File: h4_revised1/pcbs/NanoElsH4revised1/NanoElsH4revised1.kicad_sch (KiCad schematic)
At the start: 137 parts, among them Q1 SI2302ADS-T1, Q10 SI2302ADS-T1, Q11 SI2302ADS-T1, Q12 SI2302ADS-T1, Q13 SI2302ADS-T1, Q14 SI2302ADS-T1, Q15 SI2302ADS-T1, Q16 SI2302ADS-T1, Q18 SI2302ADS-T1, Q2 SI2302ADS-T1, Q3 S9013W, Q4 S9013W, Q5 SI2302ADS-T1, Q6 SI2302ADS-T1, Q7 SI2302ADS-T1, Q8 SI2302ADS-T1, Q9 SI2302ADS-T1

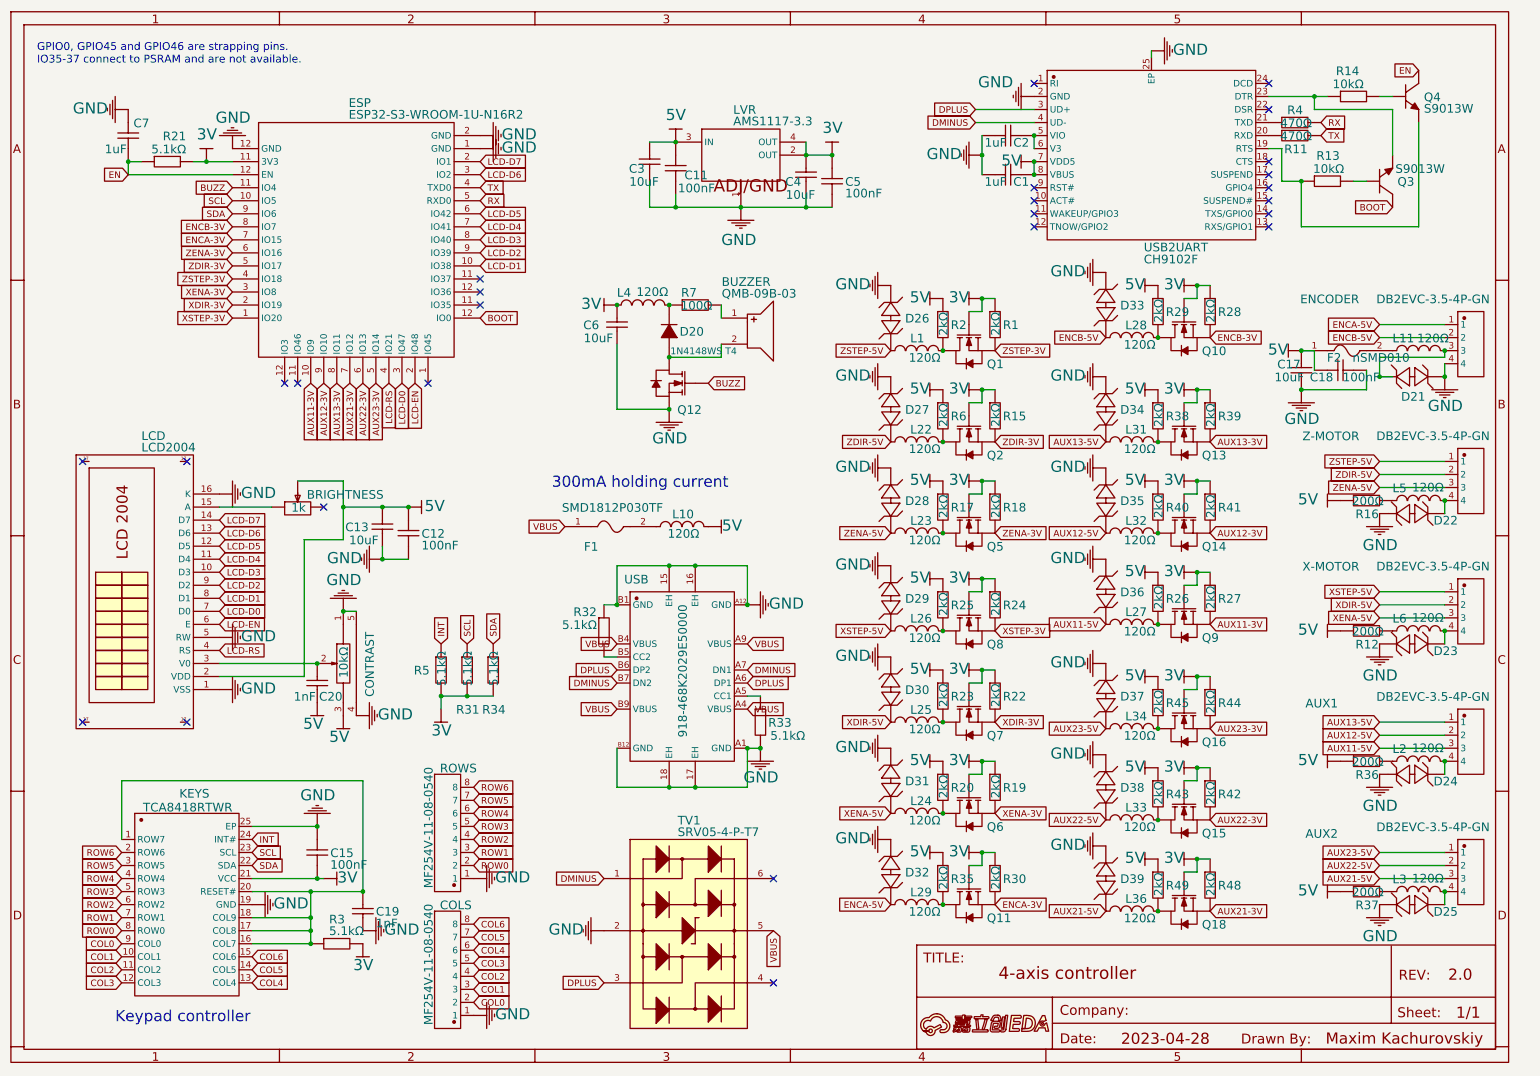
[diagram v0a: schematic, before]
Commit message: - Added actual KiCad 8 files (layout ready, but some cosmetic documentation ToDo's)
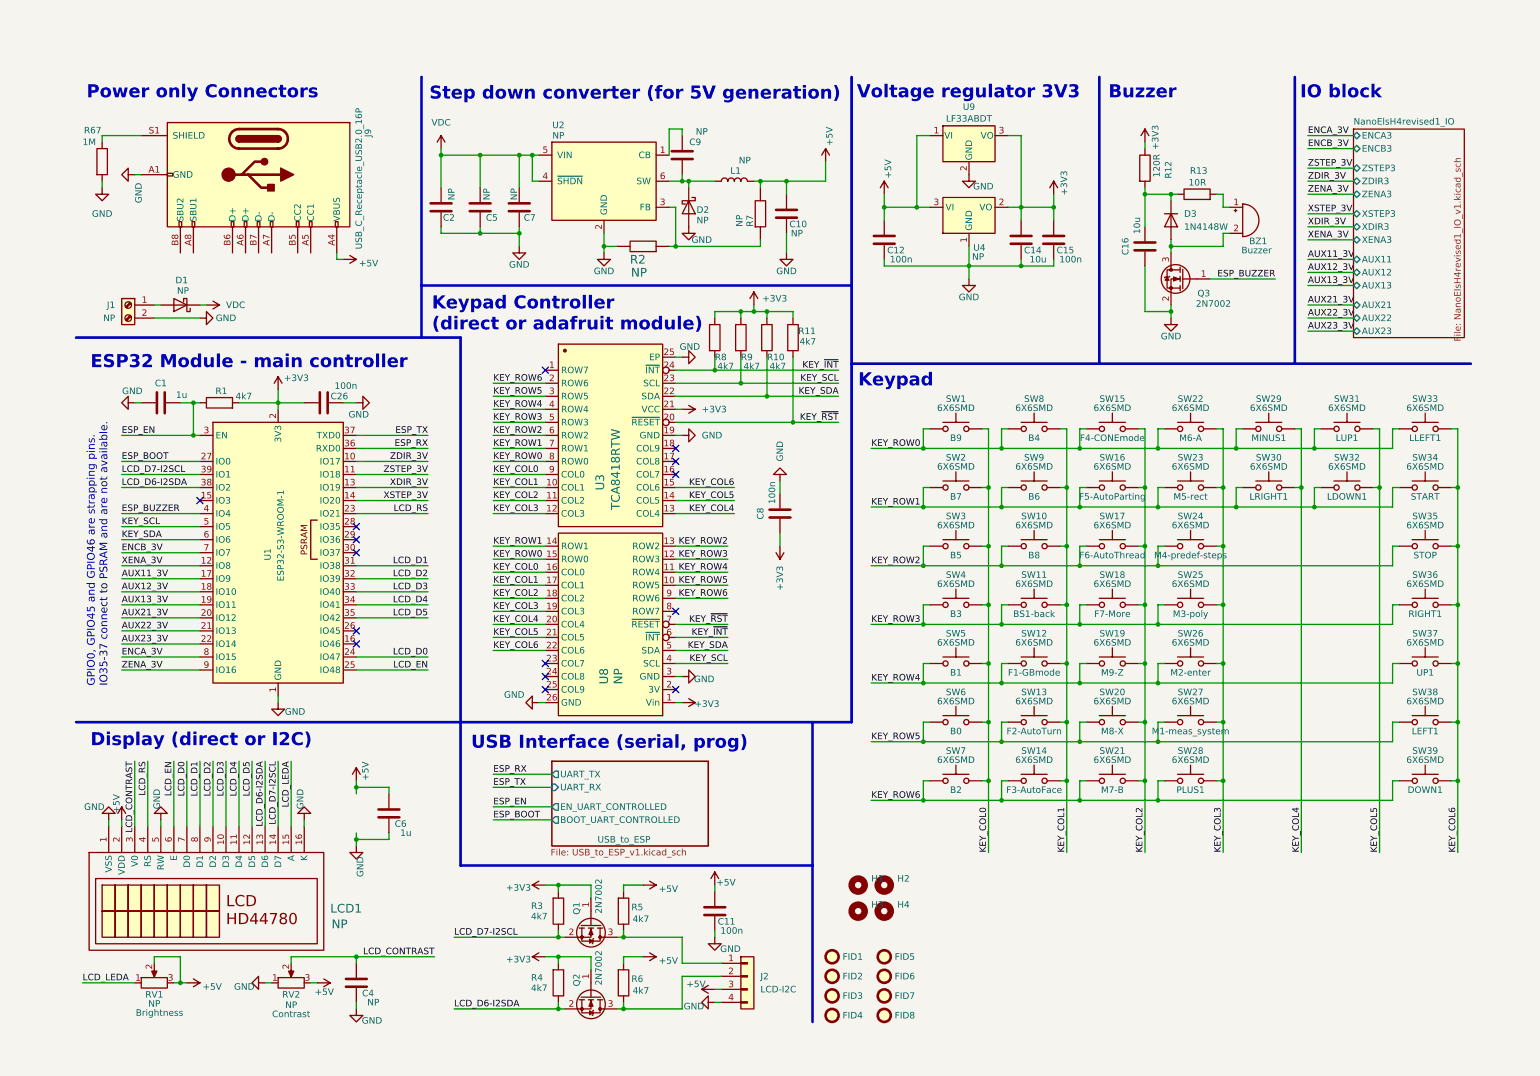
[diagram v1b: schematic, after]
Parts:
- removed A: A, symbol Unknown_10_-850
- removed AUX1: DB2EVC-3.5-4P-GN, symbol DB2EVC-3.5-4P-GN_3
- removed AUX2: DB2EVC-3.5-4P-GN, symbol DB2EVC-3.5-4P-GN_4
- removed BRIGHTNESS: 1k, symbol 3314G-2-102E
- removed BUZZER: QMB-09B-03, symbol QMB-09B-03
- removed C1: 1uF, symbol CL05A105KA5NQNC_2
- removed C11: 100nF, symbol CC0603KRX7R9BB104
- removed C12: 100nF, symbol CC0603KRX7R9BB104_3
- removed C13: 10uF, symbol CL31A106KBHNNNE_2
- removed C15: 100nF, symbol CC0603KRX7R9BB104_2
- removed C17: 10uF, symbol CL31A106KBHNNNE_3
- removed C18: 100nF, symbol CC0603KRX7R9BB104_4
- removed C19: 1nF, symbol 0402B102K500NT
- removed C2: 1uF, symbol CL05A105KA5NQNC_1
- removed C20: 1nF, symbol 0402B102K500NT_1
- removed C3: 10uF, symbol CL31A106KBHNNNE
- removed C4: 10uF, symbol CL31A106KBHNNNE_1
- removed C5: 100nF, symbol CC0603KRX7R9BB104_1
- removed C6: 10uF, symbol CL31A106KBHNNNE_4
- removed C7: 1uF, symbol CL05A105KA5NQNC
- removed COLS: MF254V-11-08-0540, symbol MF254V-11-08-0540_1
- removed CONTRAST: 10kΩ, symbol RK09K113004U
- removed D20: 1N4148WS T4, symbol 1N4148WS T4
- removed D21: KESD9B5VL, symbol KESD9B5VL
- removed D22: KESD9B5VL, symbol KESD9B5VL_1
- removed D23: KESD9B5VL, symbol KESD9B5VL_2
- removed D24: KESD9B5VL, symbol KESD9B5VL_3
- removed D25: KESD9B5VL, symbol KESD9B5VL_4
- removed D26: KESD9B5VL, symbol KESD9B5VL_5
- removed D27: KESD9B5VL, symbol KESD9B5VL_6
- removed D28: KESD9B5VL, symbol KESD9B5VL_7
- removed D29: KESD9B5VL, symbol KESD9B5VL_8
- removed D30: KESD9B5VL, symbol KESD9B5VL_9
- removed D31: KESD9B5VL, symbol KESD9B5VL_10
- removed D32: KESD9B5VL, symbol KESD9B5VL_11
- removed D33: KESD9B5VL, symbol KESD9B5VL_12
- removed D34: KESD9B5VL, symbol KESD9B5VL_13
- removed D35: KESD9B5VL, symbol KESD9B5VL_14
- removed D36: KESD9B5VL, symbol KESD9B5VL_15
- removed D37: KESD9B5VL, symbol KESD9B5VL_16
- removed D38: KESD9B5VL, symbol KESD9B5VL_17
- removed D39: KESD9B5VL, symbol KESD9B5VL_18
- removed ENCODER: DB2EVC-3.5-4P-GN, symbol DB2EVC-3.5-4P-GN_2
- removed ESP: ESP32-S3-WROOM-1U-N16R2, symbol ESP32-S3-WROOM-1U-N16R2
- removed F1: SMD1812P030TF, symbol SMD1812P030TF
- removed F2: nSMD010, symbol nSMD010
- removed KEYS: TCA8418RTWR, symbol TCA8418RTWR
- removed L1: 120Ω, symbol CBM160808U121T_4
- removed L10: 120Ω, symbol CBM160808U121T_3
- removed L11: 120Ω, symbol CBM160808U121T_2
- removed L2: 120Ω, symbol CBM160808U121T_18
- removed L22: 120Ω, symbol CBM160808U121T_5
- removed L23: 120Ω, symbol CBM160808U121T_6
- removed L24: 120Ω, symbol CBM160808U121T_7
- removed L25: 120Ω, symbol CBM160808U121T_8
- removed L26: 120Ω, symbol CBM160808U121T_9
- removed L27: 120Ω, symbol CBM160808U121T_12
- removed L28: 120Ω, symbol CBM160808U121T_10
- removed L29: 120Ω, symbol CBM160808U121T_11
- removed L3: 120Ω, symbol CBM160808U121T_19
- removed L31: 120Ω, symbol CBM160808U121T_13
- removed L32: 120Ω, symbol CBM160808U121T_14
- removed L33: 120Ω, symbol CBM160808U121T_15
- removed L34: 120Ω, symbol CBM160808U121T_16
- removed L36: 120Ω, symbol CBM160808U121T_17
- removed L4: 120Ω, symbol CBM160808U121T_20
- removed L5: 120Ω, symbol CBM160808U121T
- removed L6: 120Ω, symbol CBM160808U121T_1
- removed LCD: LCD2004, symbol LCD2004
- removed LVR: AMS1117-3.3, symbol AMS1117-3.3_C2992570
- removed Q1: SI2302ADS-T1, symbol SI2302ADS-T1
- removed Q10: SI2302ADS-T1, symbol SI2302ADS-T1_6
- removed Q11: SI2302ADS-T1, symbol SI2302ADS-T1_7
- removed Q12: SI2302ADS-T1, symbol SI2302ADS-T1_14
- removed Q13: SI2302ADS-T1, symbol SI2302ADS-T1_9
- removed Q14: SI2302ADS-T1, symbol SI2302ADS-T1_10
- removed Q15: SI2302ADS-T1, symbol SI2302ADS-T1_11
- removed Q16: SI2302ADS-T1, symbol SI2302ADS-T1_12
- removed Q18: SI2302ADS-T1, symbol SI2302ADS-T1_13
- removed Q2: SI2302ADS-T1, symbol SI2302ADS-T1_1
- removed Q3: S9013W, symbol S9013W
- removed Q4: S9013W, symbol S9013W_1
- removed Q5: SI2302ADS-T1, symbol SI2302ADS-T1_2
- removed Q6: SI2302ADS-T1, symbol SI2302ADS-T1_3
- removed Q7: SI2302ADS-T1, symbol SI2302ADS-T1_4
- removed Q8: SI2302ADS-T1, symbol SI2302ADS-T1_5
- removed Q9: SI2302ADS-T1, symbol SI2302ADS-T1_8
- removed R1: 2kΩ, symbol 0603WAF2001T5E_1
- removed R11: 470Ω, symbol 0603WAF4700T5E_1
- removed R12: 200Ω, symbol 0805W8F2000T5E_1
- removed R13: 10kΩ, symbol 0603WAF1002T5E
- removed R14: 10kΩ, symbol 0603WAF1002T5E_1
- removed R15: 2kΩ, symbol 0603WAF2001T5E_3
- removed R16: 200Ω, symbol 0805W8F2000T5E
- removed R17: 2kΩ, symbol 0603WAF2001T5E_4
- removed R18: 2kΩ, symbol 0603WAF2001T5E_5
- removed R19: 2kΩ, symbol 0603WAF2001T5E_6
- removed R2: 2kΩ, symbol 0603WAF2001T5E
- removed R20: 2kΩ, symbol 0603WAF2001T5E_7
- removed R21: 5.1kΩ, symbol 0603WAF5101T5E_6
- removed R22: 2kΩ, symbol 0603WAF2001T5E_8
- removed R23: 2kΩ, symbol 0603WAF2001T5E_9
- removed R24: 2kΩ, symbol 0603WAF2001T5E_10
- removed R25: 2kΩ, symbol 0603WAF2001T5E_11
- removed R26: 2kΩ, symbol 0603WAF2001T5E_16
- removed R27: 2kΩ, symbol 0603WAF2001T5E_17
- removed R28: 2kΩ, symbol 0603WAF2001T5E_12
- removed R29: 2kΩ, symbol 0603WAF2001T5E_13
- removed R3: 5.1kΩ, symbol 0603WAF5101T5E_5
- removed R30: 2kΩ, symbol 0603WAF2001T5E_14
- removed R31: 5.1kΩ, symbol 0603WAF5101T5E_3
- removed R32: 5.1kΩ, symbol 0603WAF5101T5E_1
- removed R33: 5.1kΩ, symbol 0603WAF5101T5E
- removed R34: 5.1kΩ, symbol 0603WAF5101T5E_4
- removed R35: 2kΩ, symbol 0603WAF2001T5E_15
- removed R36: 200Ω, symbol 0805W8F2000T5E_2
- removed R37: 200Ω, symbol 0805W8F2000T5E_3
- removed R38: 2kΩ, symbol 0603WAF2001T5E_18
- removed R39: 2kΩ, symbol 0603WAF2001T5E_19
- removed R4: 470Ω, symbol 0603WAF4700T5E
- removed R40: 2kΩ, symbol 0603WAF2001T5E_20
- removed R41: 2kΩ, symbol 0603WAF2001T5E_21
- removed R42: 2kΩ, symbol 0603WAF2001T5E_22
- removed R43: 2kΩ, symbol 0603WAF2001T5E_23
- removed R44: 2kΩ, symbol 0603WAF2001T5E_24
- removed R45: 2kΩ, symbol 0603WAF2001T5E_25
- removed R48: 2kΩ, symbol 0603WAF2001T5E_26
- removed R49: 2kΩ, symbol 0603WAF2001T5E_27
- removed R5: 5.1kΩ, symbol 0603WAF5101T5E_2
- removed R6: 2kΩ, symbol 0603WAF2001T5E_2
- removed R7: 100Ω, symbol 0805W8F1000T5E
- removed ROWS: MF254V-11-08-0540, symbol MF254V-11-08-0540
- removed TV1: SRV05-4-P-T7, symbol SRV05-4-P-T7
- removed USB: 918-468K2029E50000, symbol 918-468K2029E50000
- removed USB2UART: CH9102F, symbol CH9102F
- removed X-MOTOR: DB2EVC-3.5-4P-GN, symbol DB2EVC-3.5-4P-GN_1
- removed Z-MOTOR: DB2EVC-3.5-4P-GN, symbol DB2EVC-3.5-4P-GN
- added BZ1: Buzzer, Buzzer_Beeper:MagneticBuzzer_PUI_AT-0927-TT-6-R, symbol Device:Buzzer
- added C1, C6: 1u, Capacitor_SMD:C_0603_1608Metric, symbol Device:C
- added C10: NP, Capacitor_SMD:C_1206_3216Metric, symbol Device:C
- added C11, C12, C15, C26, C8: 100n, Capacitor_SMD:C_0603_1608Metric, symbol Device:C
- added C14, C16: 10u, Capacitor_SMD:C_1206_3216Metric, symbol Device:C
- added C2, C5: NP, Capacitor_SMD:C_1210_3225Metric, symbol Device:C
- added C4, C7, C9: NP, Capacitor_SMD:C_0603_1608Metric, symbol Device:C
- added D1: NP, Diode_SMD:D_SMA, symbol Diode:SS110
- added D2: NP, Diode_SMD:D_SMA, symbol Device:D_Schottky
- added D3: 1N4148W, Diode_SMD:D_SOD-323, symbol Device:D
- added FID1, FID2, FID3, FID4, FID5, FID6, FID7, FID8: ~, Fiducial:Fiducial_1.5mm_Mask3mm, symbol Mechanical:Fiducial
- added H1, H2, H3, H4: ~, MountingHole:MountingHole_3.2mm_M3, symbol Mechanical:MountingHole
- added J1: NP, Connector_Phoenix_MC:PhoenixContact_MCV_1,5_2-G-3.5_1x02_P3.50mm_Vertical, symbol Connector:Screw_Terminal_01x02
- added J2: LCD-I2C, Connector_PinHeader_2.54mm:PinHeader_1x04_P2.54mm_Horizontal, symbol Connector_Generic:Conn_01x04
- added J9: USB_C_Receptacle_USB2.0_16P, els_kicad_lib:USB_C_HorVert_topbot_GCT-JAE-HRO_USB4160-DX07S024WJ3R400-C31M12, symbol Connector:USB_C_Receptacle_USB2.0_16P
- added L1: NP, Inductor_SMD:L_TDK_VLS6045EX_VLS6045AF, symbol Device:L
- added LCD1: NP, els_kicad_lib:LCD_HD44780_header_horizontal, symbol els_kicad_lib:LCD_HD44780
- added Q1, Q2, Q3: 2N7002, Package_TO_SOT_SMD:SOT-23, symbol Transistor_FET:2N7002
- added R1, R10, R11, R3, R4, R5, R6, R8, R9: 4k7, Resistor_SMD:R_0603_1608Metric, symbol Device:R
- added R12: 120R, Resistor_SMD:R_0603_1608Metric, symbol Device:R
- added R13: 10R, Resistor_SMD:R_0603_1608Metric, symbol Device:R
- added R2, R7: NP, Resistor_SMD:R_0603_1608Metric, symbol 0603WAF5101T5E_6
- added R67: 1M, Resistor_SMD:R_0603_1608Metric, symbol Device:R
- added RV1, RV2: NP, Potentiometer_SMD:Potentiometer_ACP_CA6-VSMD_Vertical, symbol Device:R_Potentiometer
- added SW1, SW10, SW11, SW12, SW13, SW14, SW15, SW16, SW17, SW18, SW19, SW2, SW20, SW21, SW22, SW23, SW24, SW25, SW26, SW27, SW28, SW29, SW3, SW30, SW31, SW32, SW33, SW34, SW35, SW36, SW37, SW38, SW39, SW4, SW5, SW6, SW7, SW8, SW9: 6X6SMD, Button_Switch_SMD:SW_Push_1P1T_NO_6x6mm_H9.5mm, symbol Switch:SW_Push
- added U1: ESP32-S3-WROOM-1, els_kicad_lib:ESP32-S3-WROOM-1_bighole, symbol RF_Module:ESP32-S3-WROOM-1
- added U2: NP, Package_TO_SOT_SMD:SOT-23-6, symbol Regulator_Switching:LMR16006YQ
- added U3: TCA8418RTW, Package_DFN_QFN:WQFN-24-1EP_4x4mm_P0.5mm_EP2.45x2.45mm, symbol els_kicad_lib:TCA8418
- added U4: NP, Package_TO_SOT_SMD:SOT-223-3_TabPin2, symbol Regulator_Linear:AMS1117-3.3
- added U8: NP, els_kicad_lib:Adafruit_STEMMA_TCA8418, symbol els_kicad_lib:Adafruit_STEMMA_TCA8418
- added U9: LF33ABDT, Package_TO_SOT_SMD:TO-252-2, symbol Regulator_Linear:LF33_TO252
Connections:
- net GND: now also C1.1, C10.1, C11.1, C12.1, C14.1, C15.1, C16.1, C2.1, C26.1, C4.1, C5.1, C6.1, C7.1, C8.2, D2.2 (A), J1.2 (Pin_2), J2.4 (Pin_4), J9.A1 (GND), J9.A12 (GND), J9.B1 (GND), J9.B12 (GND), LCD1.1 (VSS), LCD1.16 (K), LCD1.5 (RW), Q3.2 (S), R2.1, R67.2, RV2.1, U1.1 (GND), U1.40 (GND), U1.41 (GND), U2.2 (GND), U3.19 (GND), U3.25 (EP), U4.1 (GND), U8.26 (GND), U8.3 (GND), U9.2 (GND)
- new net: J2.1 (Pin_1), Q1.3 (D), R5.1
- new net: C16.2, D3.1 (K), R12.2, R13.1
- new net: BZ1.2 (-), D3.2 (A), Q3.3 (D)
- new net: C9.1, D2.1 (K), L1.1, U2.6 (SW)
- new net: C9.2, U2.1 (CB)
- new net: D1.2 (A), J1.1 (Pin_1)
- new net: J9.S1 (SHIELD), R67.1
- new net: BZ1.1 (+), R13.2
- new net: R2.2, R7.2, U2.3 (FB)
- new net: J2.2 (Pin_2), Q2.3 (D), R6.1
- new net +3V3: C14.2, C15.2, C26.2, C8.1, Q1.1 (G), Q2.1 (G), R1.2, R10.1, R11.1, R12.1, R3.2, R4.2, R8.1, R9.1, U1.2 (3V3), U3.21 (VCC), U4.2 (VO), U8.1 (Vin), U9.3 (VO)
- new net +5V: C10.2, C11.2, C12.2, C6.2, J2.3 (Pin_3), J9.A4 (VBUS), J9.A9 (VBUS), J9.B4 (VBUS), J9.B9 (VBUS), L1.2, LCD1.2 (VDD), R5.2, R6.2, R7.1, RV1.2, RV1.3, RV2.3, U4.3 (VI), U9.1 (VI)
- new net AUX11_3V: U1.17 (IO9)
- new net AUX12_3V: U1.18 (IO10)
- new net AUX13_3V: U1.19 (IO11)
- new net AUX21_3V: U1.20 (IO12)
- new net AUX22_3V: U1.21 (IO13)
- new net AUX23_3V: U1.22 (IO14)
- new net ENCA_3V: U1.8 (IO15)
- new net ENCB_3V: U1.7 (IO7)
- new net ESP_BOOT: U1.27 (IO0)
- new net ESP_BUZZER: Q3.1 (G), U1.4 (IO4)
- new net ESP_EN: C1.2, R1.1, U1.3 (EN)
- new net ESP_RX: U1.36 (RXD0)
- new net ESP_TX: U1.37 (TXD0)
- new net KEY_COL0: SW1.2, SW2.2, SW3.2, SW4.2, SW5.2, SW6.2, SW7.2, U3.9 (COL0), U8.16 (COL0)
- new net KEY_COL1: SW10.2, SW11.2, SW12.2, SW13.2, SW14.2, SW8.2, SW9.2, U3.10 (COL1), U8.17 (COL1)
- new net KEY_COL2: SW15.2, SW16.2, SW17.2, SW18.2, SW19.2, SW20.2, SW21.2, U3.11 (COL2), U8.18 (COL2)
- new net KEY_COL3: SW22.2, SW23.2, SW24.2, SW25.2, SW26.2, SW27.2, SW28.2, U3.12 (COL3), U8.19 (COL3)
- new net KEY_COL4: SW29.2, SW30.2, U3.13 (COL4), U8.20 (COL4)
- new net KEY_COL5: SW31.2, SW32.2, U3.14 (COL5), U8.21 (COL5)
- new net KEY_COL6: SW33.2, SW34.2, SW35.2, SW36.2, SW37.2, SW38.2, SW39.2, U3.15 (COL6), U8.22 (COL6)
- new net KEY_ROW0: SW1.1, SW15.1, SW22.1, SW29.1, SW31.1, SW33.1, SW8.1, U3.8 (ROW0), U8.15 (ROW0)
- new net KEY_ROW1: SW16.1, SW2.1, SW23.1, SW30.1, SW32.1, SW34.1, SW9.1, U3.7 (ROW1), U8.14 (ROW1)
- new net KEY_ROW2: SW10.1, SW17.1, SW24.1, SW3.1, SW35.1, U3.6 (ROW2), U8.13 (ROW2)
- new net KEY_ROW3: SW11.1, SW18.1, SW25.1, SW36.1, SW4.1, U3.5 (ROW3), U8.12 (ROW3)
- new net KEY_ROW4: SW12.1, SW19.1, SW26.1, SW37.1, SW5.1, U3.4 (ROW4), U8.11 (ROW4)
- new net KEY_ROW5: SW13.1, SW20.1, SW27.1, SW38.1, SW6.1, U3.3 (ROW5), U8.10 (ROW5)
- new net KEY_ROW6: SW14.1, SW21.1, SW28.1, SW39.1, SW7.1, U3.2 (ROW6), U8.9 (ROW6)
- new net KEY_SCL: R9.2, U1.5 (IO5), U3.23 (SCL), U8.4 (SCL)
- new net KEY_SDA: R10.2, U1.6 (IO6), U3.22 (SDA), U8.5 (SDA)
- new net KEY_~{INT}: R8.2, U3.24 (~{INT}), U8.6 (~{INT})
- new net KEY_~{RST}: R11.2, U3.20 (~{RESET}), U8.7 (~{RESET})
- new net LCD_CONTRAST: C4.2, LCD1.3 (V0), RV2.2
- new net LCD_D0: LCD1.7 (D0), U1.24 (IO47)
- new net LCD_D1: LCD1.8 (D1), U1.31 (IO38)
- new net LCD_D2: LCD1.9 (D2), U1.32 (IO39)
- new net LCD_D3: LCD1.10 (D3), U1.33 (IO40)
- new net LCD_D4: LCD1.11 (D4), U1.34 (IO41)
- new net LCD_D5: LCD1.12 (D5), U1.35 (IO42)
- new net LCD_D6-I2SDA: LCD1.13 (D6), Q2.2 (S), R4.1, U1.38 (IO2)
- new net LCD_D7-I2SCL: LCD1.14 (D7), Q1.2 (S), R3.1, U1.39 (IO1)
- new net LCD_EN: LCD1.6 (E), U1.25 (IO48)
- new net LCD_LEDA: LCD1.15 (A), RV1.1
- new net LCD_RS: LCD1.4 (RS), U1.23 (IO21)
- new net VDC: C2.2, C5.2, C7.2, D1.1 (K), U2.4 (~{SHDN}), U2.5 (VIN)
- new net XDIR_3V: U1.13 (IO19)
- new net XENA_3V: U1.12 (IO8)
- new net XSTEP_3V: U1.14 (IO20)
- new net ZDIR_3V: U1.10 (IO17)
- new net ZENA_3V: U1.9 (IO16)
- new net ZSTEP_3V: U1.11 (IO18)
- no-connect marks 26 -> 15
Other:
- added sheet NanoElsH4revised1_IO (NanoElsH4revised1_IO_v1.kicad_sch)
- added sheet USB_to_ESP (USB_to_ESP_v1.kicad_sch)
- note added: "Buzzer"
- note added: "Display (direct or I2C)"
- note added: "ESP32 Module - main controller"
- note added: "IO block"
- note added: "Keypad"
- note added: "Keypad Controller (direct or adafruit module)"
- note added: "Power only Connectors"
- note added: "Step down converter (for 5V generation)"
- note added: "USB Interface (serial, prog)"
- note added: "Voltage regulator 3V3"
- note removed: "300mA holding current"
- note removed: "Keypad controller"
